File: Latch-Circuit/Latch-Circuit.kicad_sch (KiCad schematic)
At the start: 112 parts, among them J1 BM02B-PASS-1-TF, J10 BM02B-PASS-1-TF, J2 BM03B-PASS-1-TF, J3 BM02B-PASS-1-TF, J4 BM02B-PASS-1-TF, J5 BM02B-PASS-1-TF, J6 BM02B-PASS-1-TF, J7 B2P-VH, J8 BM02B-PASS-1-TF, J9 BM02B-PASS-1-TF, K1 G5Q-1A4_DC12, K2 G5Q-1A4_DC12, K3 G5Q-1A4_DC12, Q1 DMP3098LQ-7, Q10 2N7002K-AU, Q11 2N7002K-AU, Q12 PJA3439-AU_R1_000A1, Q13 PJA3439-AU_R1_000A1, Q14 2N7002K-AU, Q15 2N7002K-AU, Q16 2N7002K-AU, Q17 2N7002K-AU, Q18 2N7002K-AU, Q19 2N7002K-AU, Q2 2N7002K-AU, Q3 PJA3439-AU_R1_000A1, Q4 2N7002K-AU, Q5 PJA3439-AU_R1_000A1, Q6 2N7002K-AU, Q7 2N7002K-AU, Q8 PJA3439-AU_R1_000A1, Q9 PJA3439-AU_R1_000A1

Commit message: re-annotation
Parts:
- renumbered D8 to D2, D2 to D3, D3 to D4, D9 to D5, D4 to D6, D5 to D7, D6 to D8, D7 to D9, Q18 to Q10, Q6 to Q11, Q7 to Q12, Q8 to Q13, Q9 to Q14, Q19 to Q15, Q10 to Q16, Q11 to Q17, Q12 to Q18, Q13 to Q19, Q14 to Q2, Q15 to Q3, Q2 to Q4, Q3 to Q5, Q16 to Q6, Q4 to Q7, Q5 to Q8, Q17 to Q9, R37 to R1, R11 to R10, R5 to R11, R34 to R12, R6 to R13, R39 to R14, R40 to R15, R7 to R16, R8 to R17, R9 to R18, R41 to R19, R1 to R2, R42 to R20, R10 to R21, R47 to R22, R30 to R23, R43 to R24, R44 to R25, R12 to R26, R13 to R27, R14 to R28, R15 to R29, R38 to R3, R45 to R30, R46 to R31, R16 to R32, R17 to R33, R18 to R34, R19 to R35, R31 to R36, R20 to R37, R21 to R38, R22 to R39, R35 to R4, R23 to R40, R24 to R41, R25 to R42, R26 to R43, R27 to R44, R28 to R45, R29 to R46, R48 to R47, R49 to R48, R32 to R49, R33 to R5, R2 to R6, R36 to R7, R3 to R8, R4 to R9

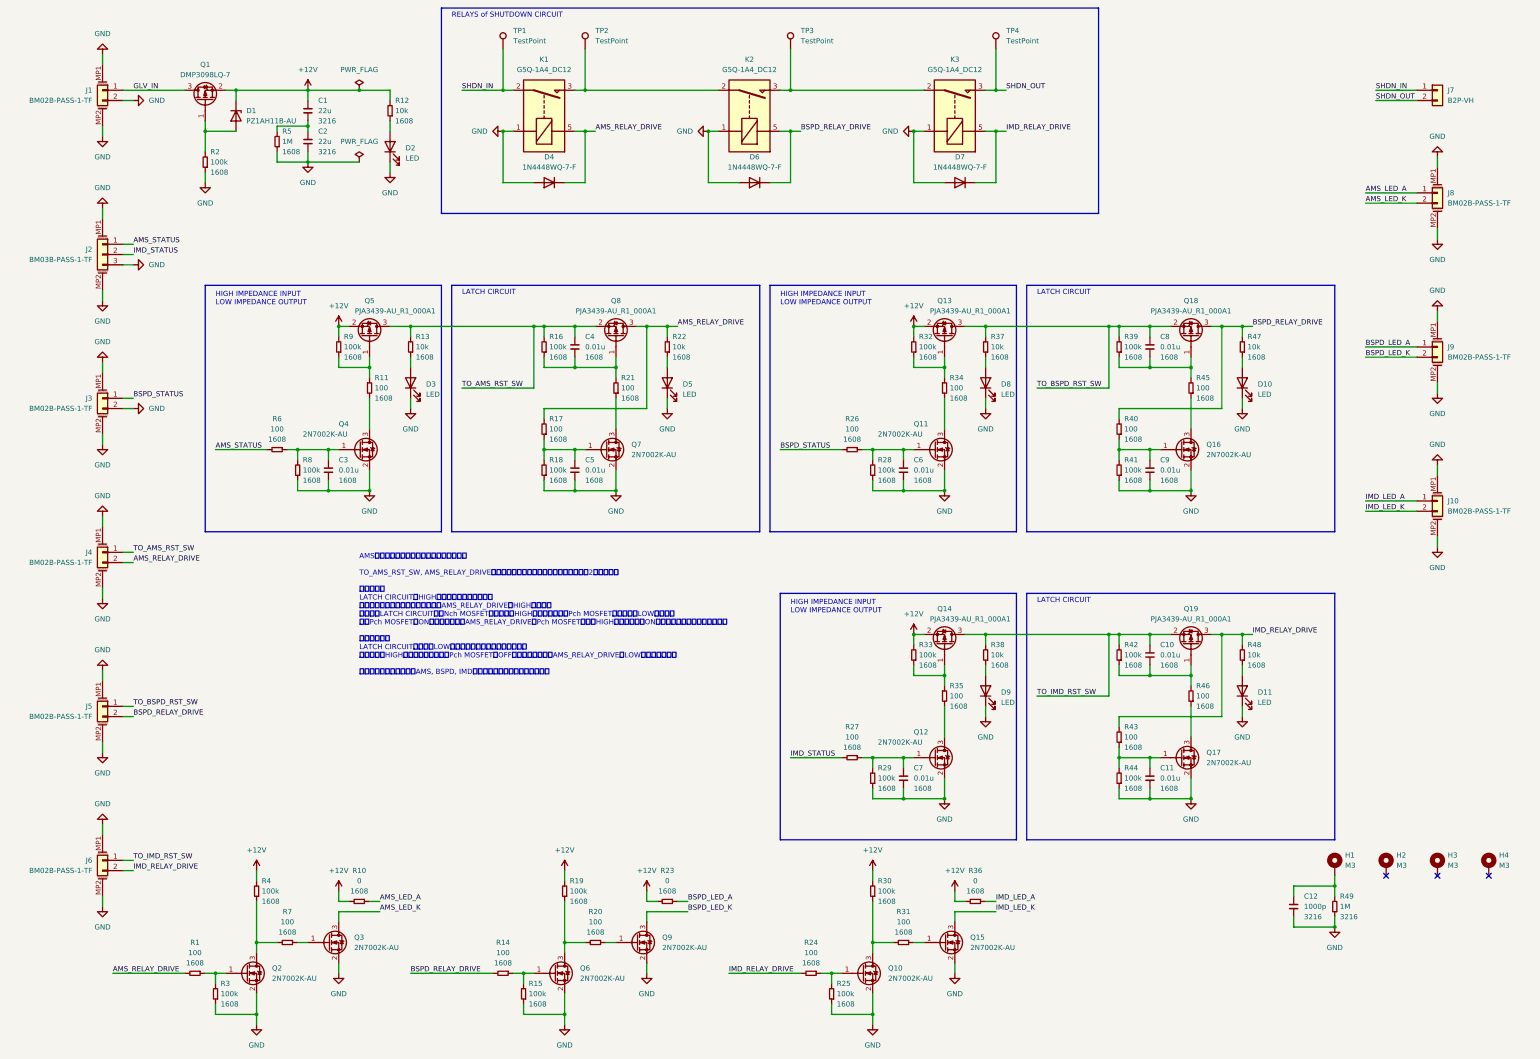
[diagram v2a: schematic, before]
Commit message: Name changed from AMS to BMS
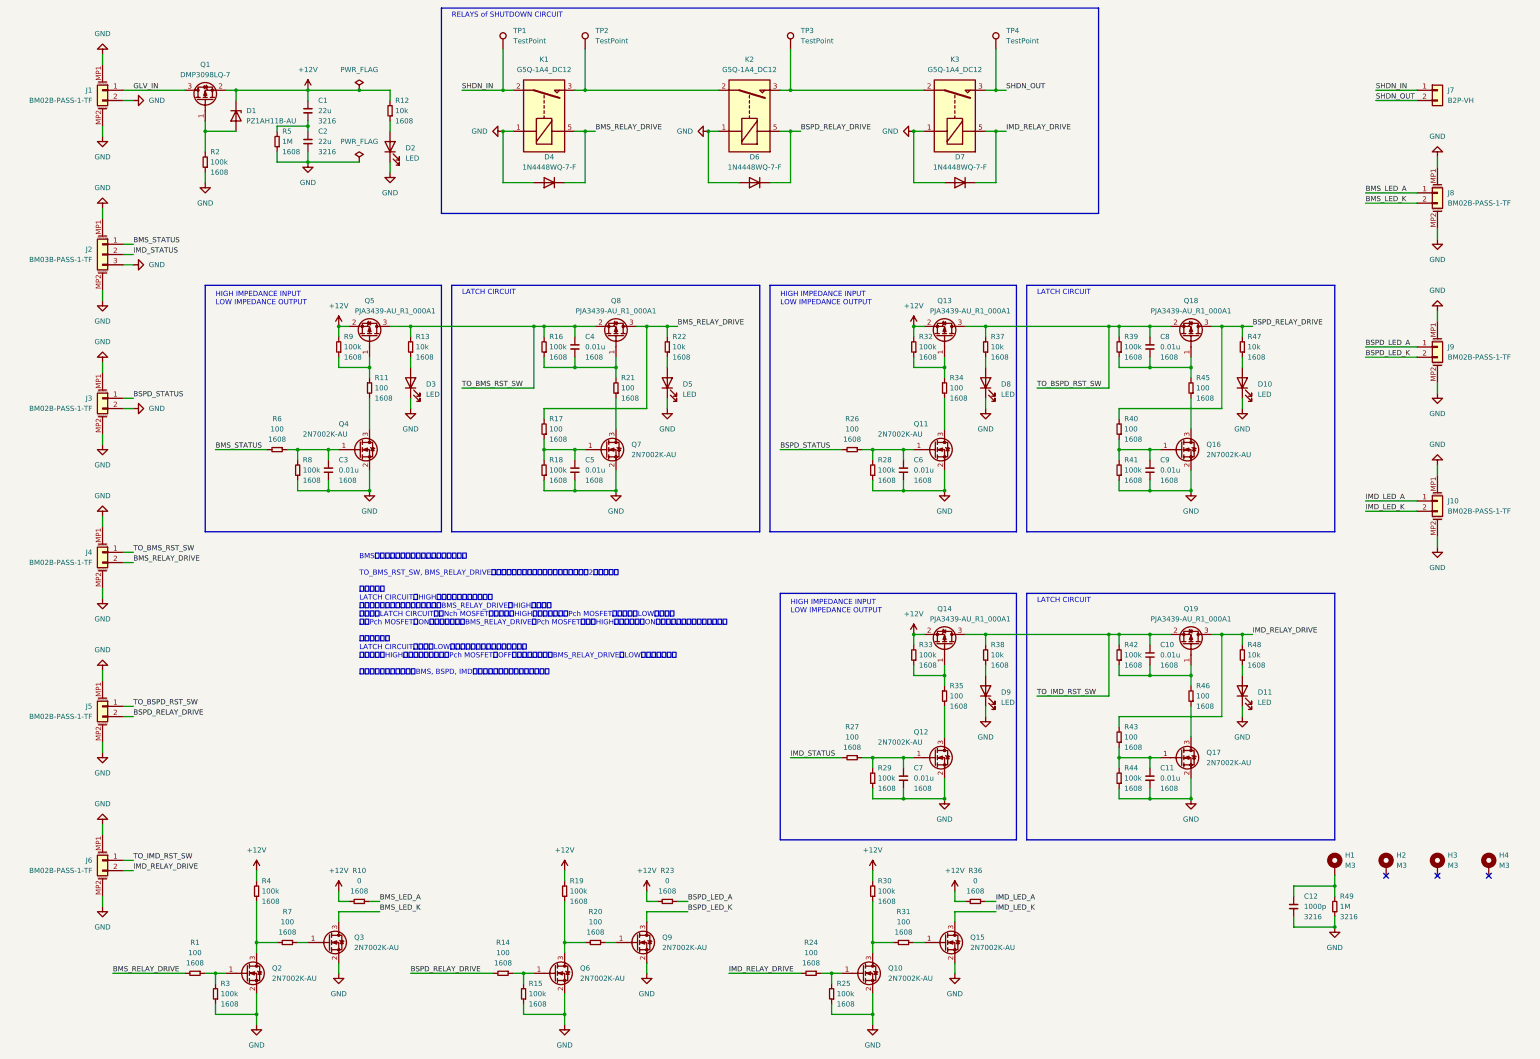
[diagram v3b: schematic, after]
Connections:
- net AMS_LED_A renamed BMS_LED_A
- net AMS_LED_K renamed BMS_LED_K
- net AMS_RELAY_DRIVE renamed BMS_RELAY_DRIVE
- net AMS_STATUS renamed BMS_STATUS
- net TO_AMS_RST_SW renamed TO_BMS_RST_SW
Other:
- note added: "BMSのラッチ回路を例に、動作を説明する。 TO_BMS_RST_SW, BMS_RELAY_DRIVE間にはプッシュスイッチが実装される。他2つも同様。 セット動作 LATCH CIRCUITにHIGHが入力されているとき、 プッシュスイッチを押すと一時的にBMS_RELAY_DRIVEがHIGHとなる。 そして、LATCH CIRCUIT下側Nch MOSFETのゲートがHIGHになると、上側Pch MOSFETのゲートがLOWになる。 一度Pch MOSFETをONしてしまえば、BMS_RELAY_DRIVEはPch MOSFETによりHIGHとなるので、ON状態を保持することができる。 リセット動作 LATCH CIRCUITの入力をLOWにすることで、リセットされる。 再び入力がHIGHになったとしても、Pch MOSFETはOFF状態であるため、BMS_RELAY_DRIVE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"
- note removed: "AMSのラッチ回路を例に、動作を説明する。 TO_AMS_RST_SW, AMS_RELAY_DRIVE間にはプッシュスイッチが実装される。他2つも同様。 セット動作 LATCH CIRCUITにHIGHが入力されているとき、 プッシュスイッチを押すと一時的にAMS_RELAY_DRIVEがHIGHとなる。 そして、LATCH CIRCUIT下側Nch MOSFETのゲートがHIGHになると、上側Pch MOSFETのゲートがLOWになる。 一度Pch MOSFETをONしてしまえば、AMS_RELAY_DRIVEはPch MOSFETによりHIGHとなるので、ON状態を保持することができる。 リセット動作 LATCH CIRCUITの入力をLOWにすることで、リセットされる。 再び入力がHIGHになったとしても、Pch MOSFETはOFF状態であるため、AMS_RELAY_DRIVE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"
